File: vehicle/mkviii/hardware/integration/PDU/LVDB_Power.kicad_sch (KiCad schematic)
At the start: 27 parts

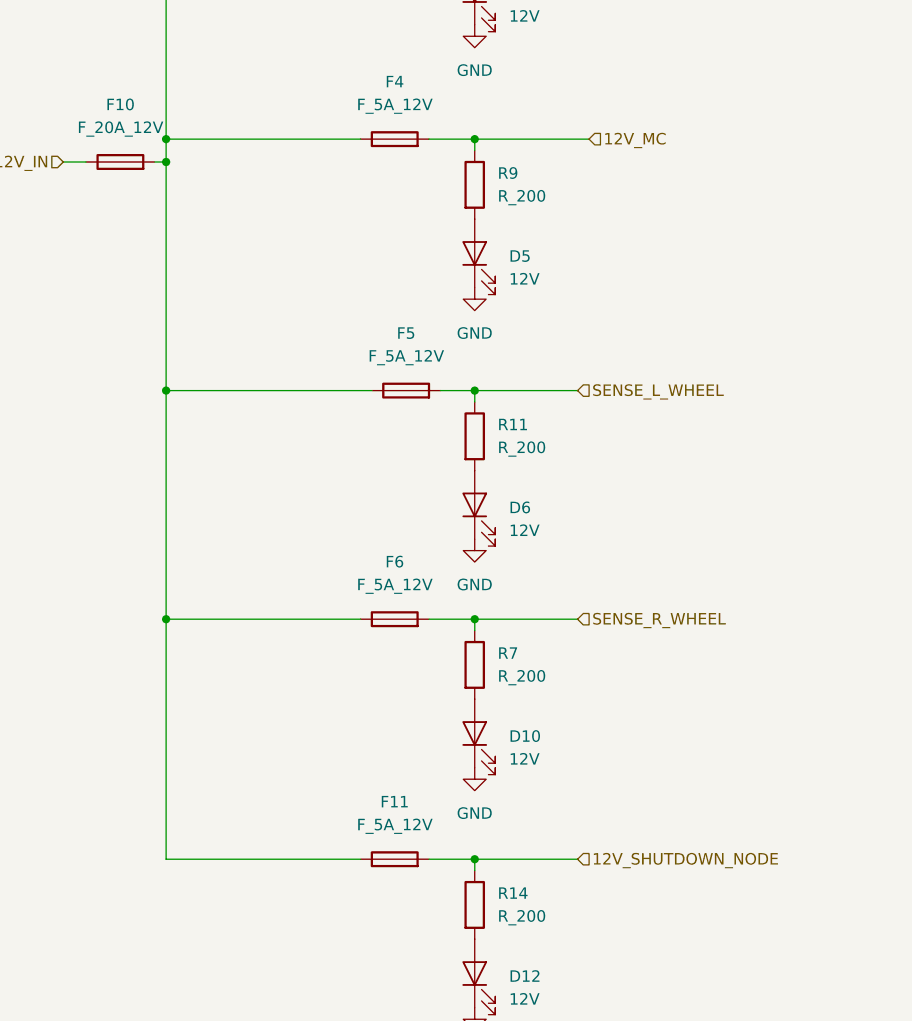
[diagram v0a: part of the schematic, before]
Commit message: Yeet unused wheel speed sense pins
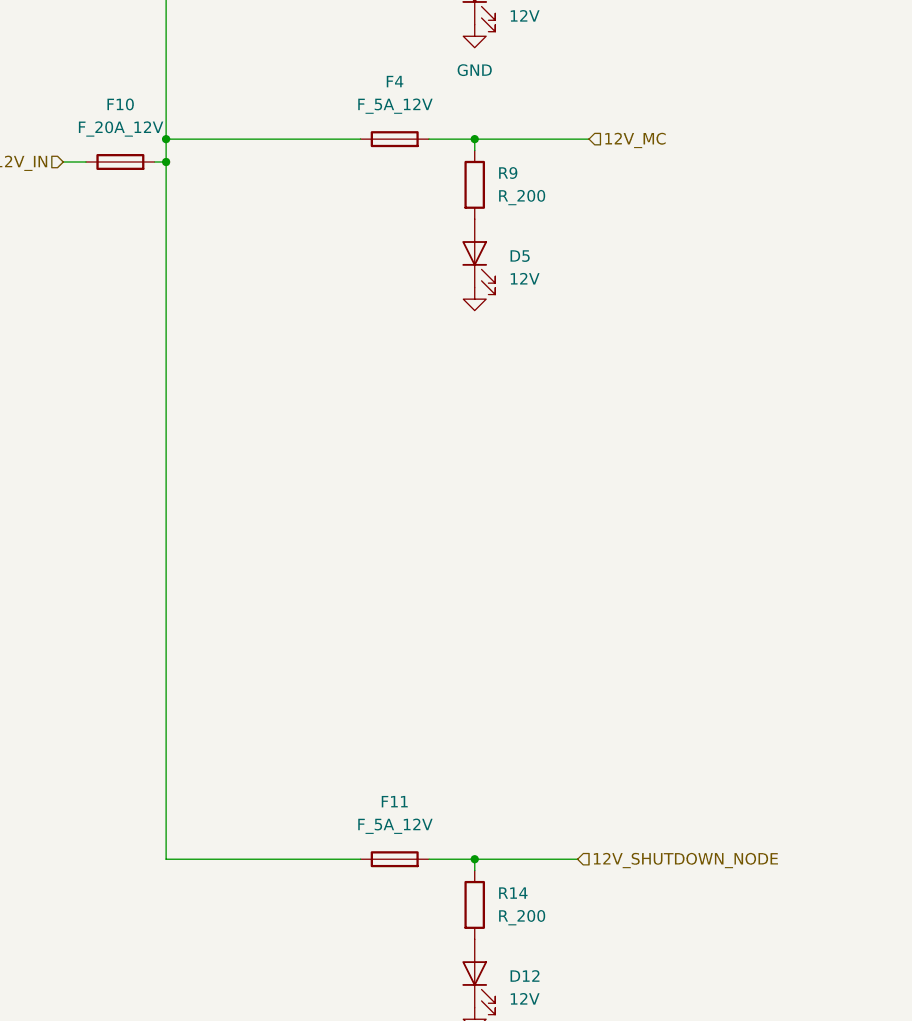
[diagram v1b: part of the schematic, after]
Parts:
- removed D10, D6: 12V, LED_SMD:LED_0805_2012Metric, symbol oem:LED_0805
- removed F5, F6: F_5A_12V, Fuse:Fuse_1210_3225Metric, symbol OEM:F_500mA_16V
- removed R11, R7: R_200, Resistor_SMD:R_0201_0603Metric, symbol OEM:R_200
